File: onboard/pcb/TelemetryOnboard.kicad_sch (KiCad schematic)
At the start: 141 parts, among them J1 USB-C, J2 USB-C, J3 RFPC-SMA28-F, J4 RFPC-SMA28-F, M1 M4 Mounting Hole, M2 M4 Mounting Hole, M3 M4 Mounting Hole, M4 M4 Mounting Hole, Q1 NPN, U1 CP2102N, U2 CP2102N, U3 RC1780HP-RC232, U4 RC1701HP-RC232, U5 AVR128DB64x-xPT, U6 W25Q80DVSSIG

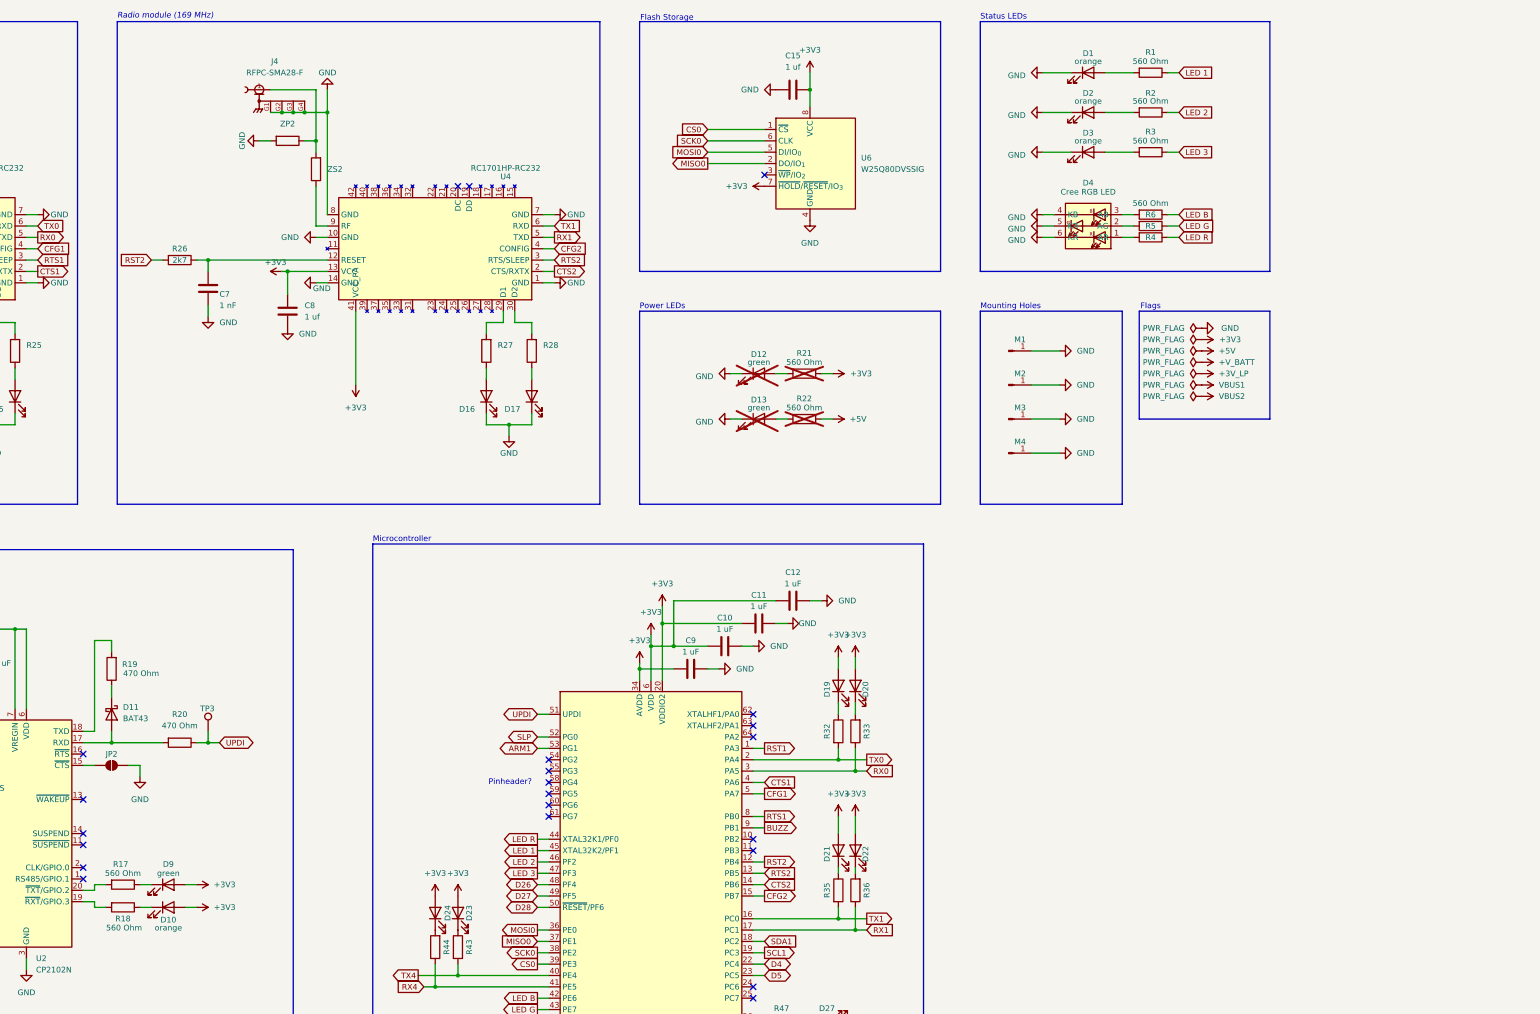
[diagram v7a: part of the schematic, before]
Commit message: change usb connector and add tvs diode
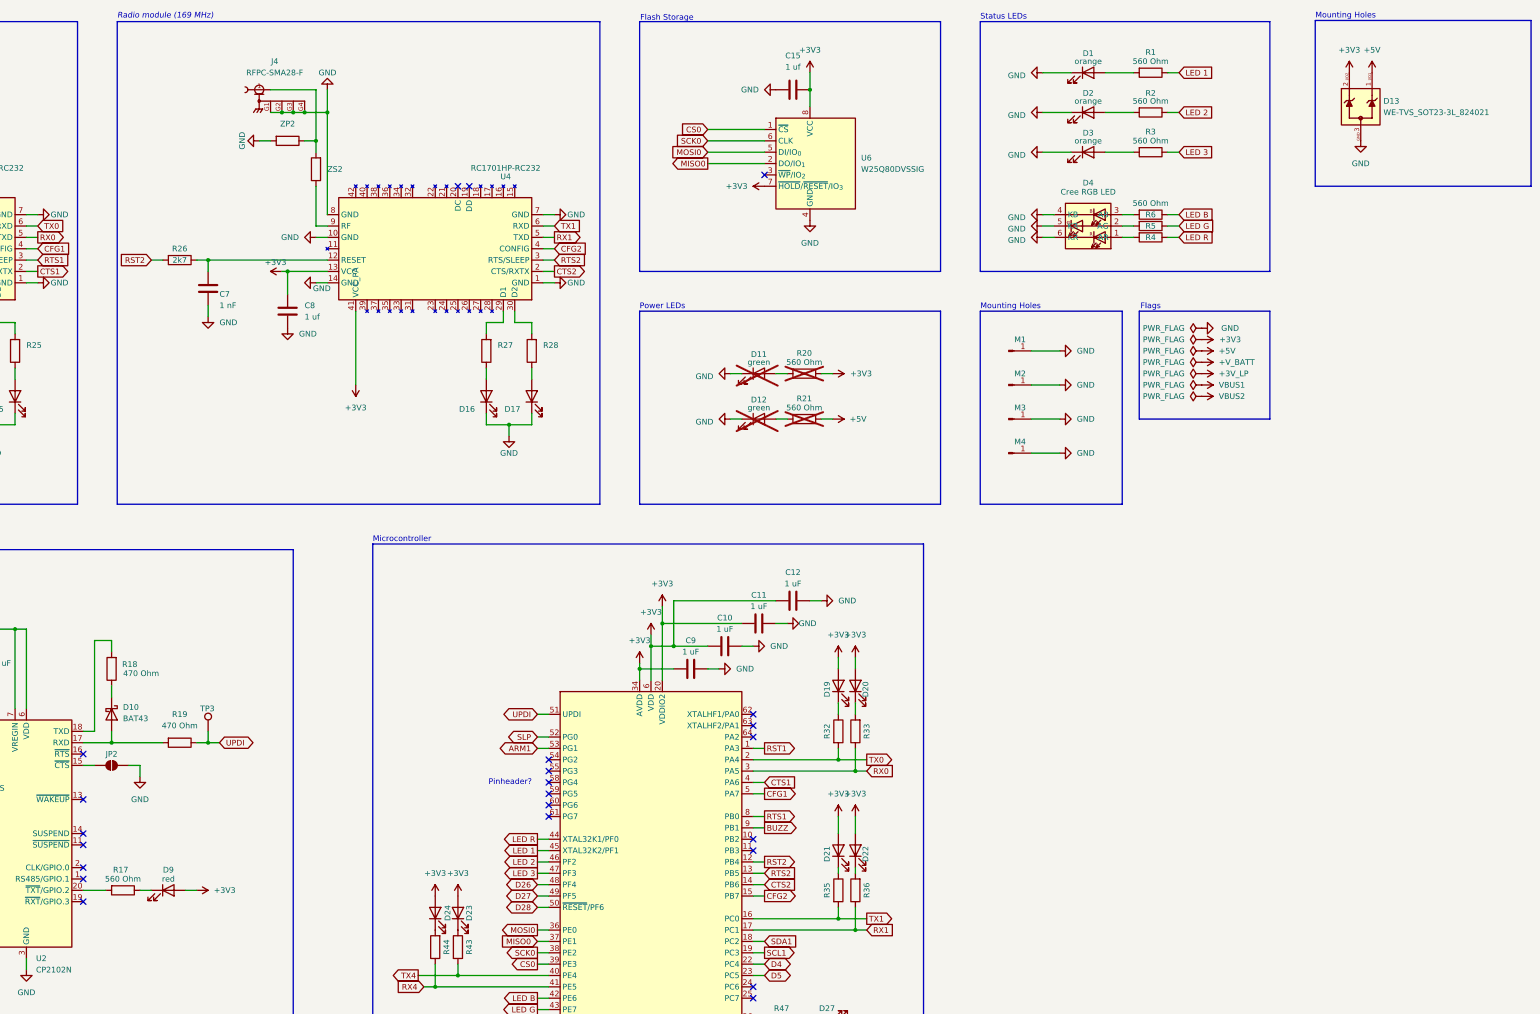
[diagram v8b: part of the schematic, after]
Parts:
- removed D10: orange, LED_SMD:LED_0805_2012Metric_Pad1.15x1.40mm_HandSolder, symbol Device:LED
- removed R18: 560 Ohm, Resistor_SMD:R_0805_2012Metric_Pad1.20x1.40mm_HandSolder, symbol Device:R
- added D13: WE-TVS_SOT23-3L_824021, Package_TO_SOT_SMD:SOT-23-3, symbol Symbols:WE-TVS_SOT23-3L_824021
- D9: value green -> red
- J1, J2: footprint Footprints:GCT_USB4215-03-A_REVA -> Footprints:GCT_USB4216-03-A_REVA; symbol Symbols:USB4215-03-A_REVA -> Symbols:USB4216-03-A_REVA
- renumbered D11 to D10, D12 to D11, D13 to D12, R19 to R18, R20 to R19, R21 to R20, R22 to R21
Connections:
- net +3V3: now also D13.2
- net +5V: now also D13.1
- net GND: now also D13.3
- no-connect marks 40 -> 41
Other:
- moved on the sheet: D9, R17
